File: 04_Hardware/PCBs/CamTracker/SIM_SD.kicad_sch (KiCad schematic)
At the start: 49 parts, among them J13 SIM8066-6-1-14-01-A, J14 MEM2061-01-188-00-A, U1 SC206EEMDA-G51-UGNDA, U11 ST4SI2M0020TPIFW

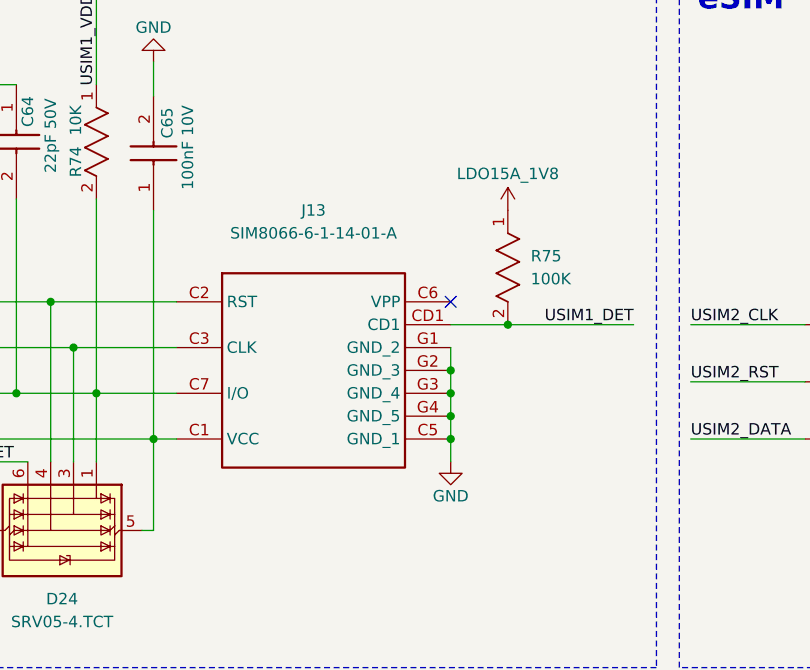
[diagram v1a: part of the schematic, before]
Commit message: feat(PCB): Added TE Connectivity connectors except the SD connector
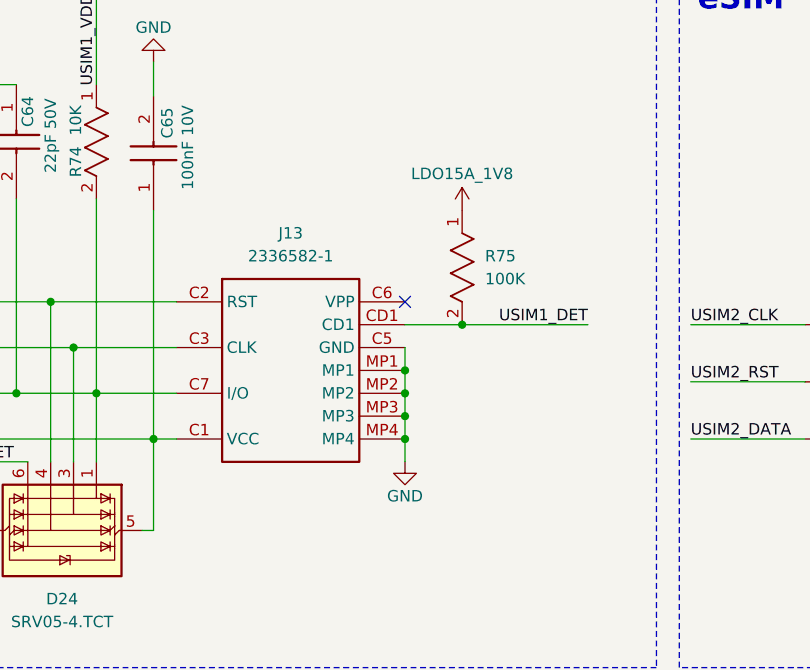
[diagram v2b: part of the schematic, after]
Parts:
- removed J13: SIM8066-6-1-14-01-A, 000MCLib:SIM8066611401A, symbol 000MCLib:SIM8066-6-1-14-01-A
- added J13: 2336582-1, 000MCLib:23365821, symbol 000MCLib:2336582-1
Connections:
- net GND: now also J13.C5 (GND), J13.MP1, J13.MP2, J13.MP3, J13.MP4
- net USIM1_DET: now also J13.CD1
- net USIM1_VDD: now also J13.C1 (VCC)
- net at C64.2, D24.1 (I/O1), R67.1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: now also J13.C7 (I/O)
- net at C63.2, D24.3 (I/O2), R66.1: now also J13.C3 (CLK)
- net at C62.2, D24.4 (I/O3), R65.1: now also J13.C2 (RST)
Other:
- moved on the sheet: R75

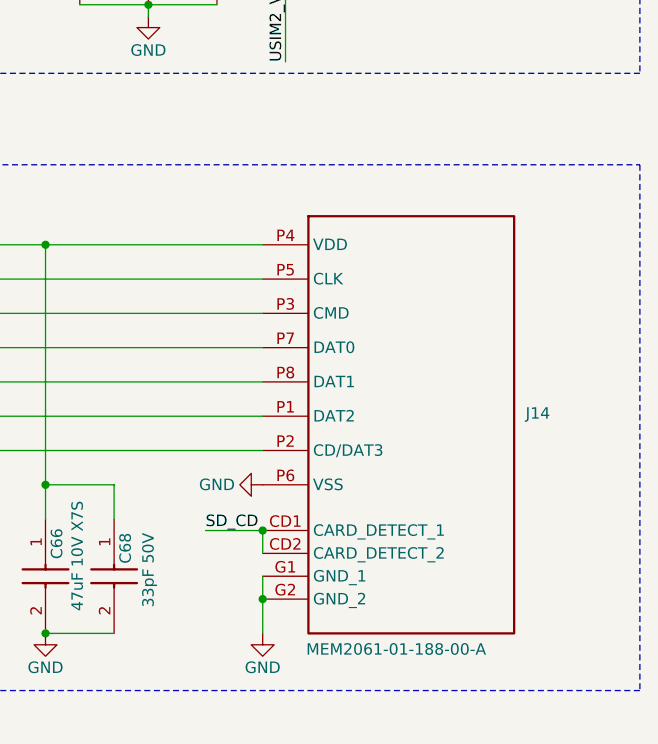
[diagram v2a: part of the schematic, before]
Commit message: feat(PCB): Cam Connectors have been changed with 2x10P
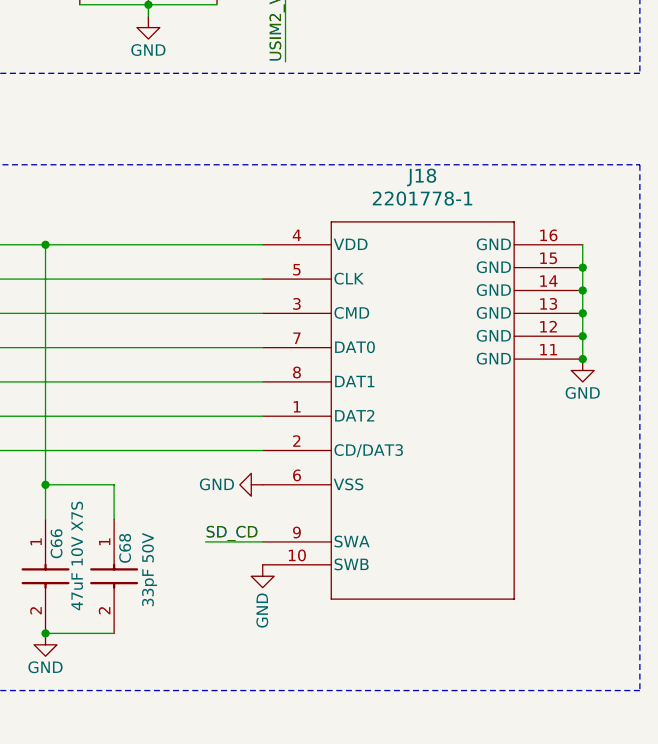
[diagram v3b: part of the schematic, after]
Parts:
- removed J14: MEM2061-01-188-00-A, 000MCLib:MEM20610118800A, symbol 000MCLib:MEM2061-01-188-00-A
- added J18: 2201778-1, 000MCLib:2201778-1_TEC, symbol 000MCLib:2201778-1
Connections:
- net GND: now also J18.10 (SWB), J18.11 (GND), J18.12 (GND), J18.13 (GND), J18.14 (GND), J18.15 (GND), J18.16 (GND), J18.6 (VSS)
- net SD_CD: now also J18.9 (SWA)
- net SD_VDD: now also J18.4 (VDD)
- net at D30.1, R73.1, R80.1: now also J18.2 (CD/DAT3)
- net at D29.1, R72.1, R79.1: now also J18.1 (DAT2)
- net at D26.1, R69.1, R76.1: now also J18.3 (CMD)
- net at D28.1, R71.1, R78.1: now also J18.8 (DAT1)
- net at D25.1, R68.1: now also J18.5 (CLK)
- net at D27.1, R70.1, R77.1: now also J18.7 (DAT0)
